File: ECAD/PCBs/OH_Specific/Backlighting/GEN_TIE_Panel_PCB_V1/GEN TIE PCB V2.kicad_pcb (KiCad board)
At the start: 2 copper layers, 45.7 x 130.8 mm, 28 parts, among them J1 IN, J2 THRU

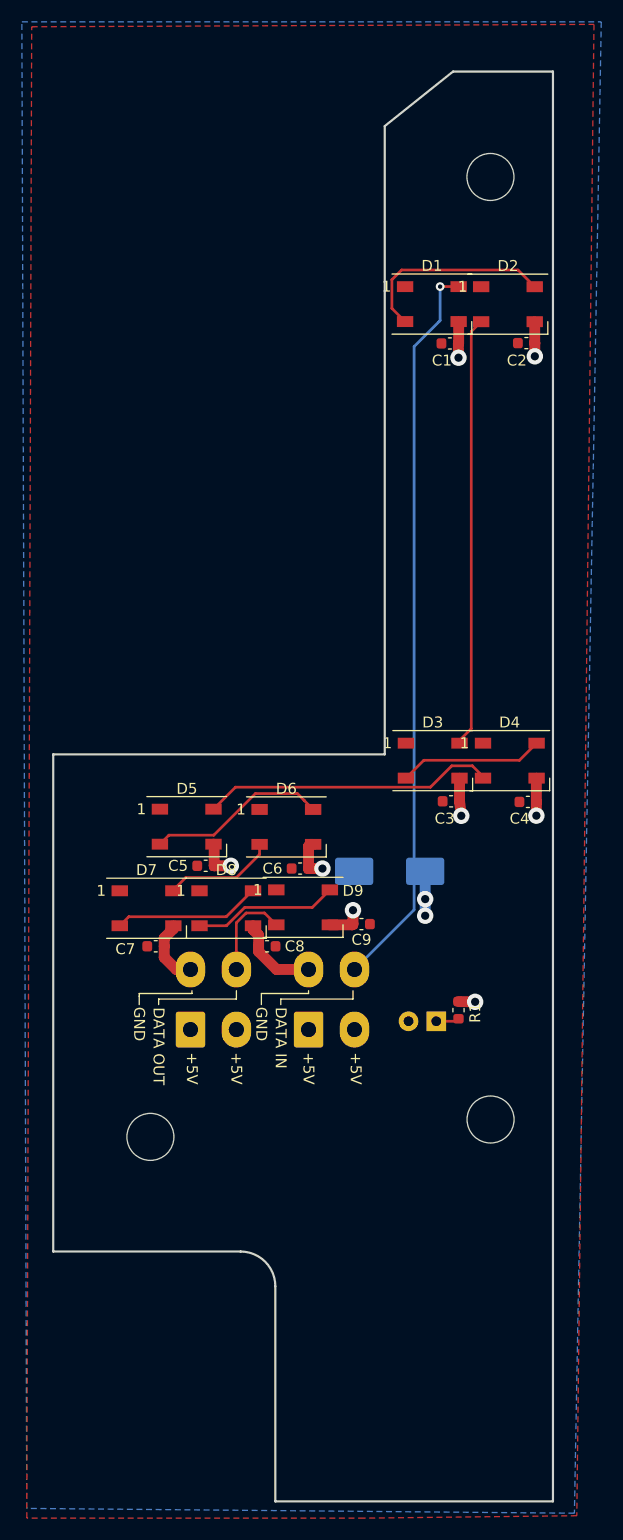
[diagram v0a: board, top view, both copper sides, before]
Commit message: GEN TIE Panel Backlighting Update
Changed - Data in trace re-routed so as not go straight through the capacitor pad, shorting it to 5V.
Changed - Manufacturing files to match the update
Changed - Version from 1.0 to 2.1 to match the other PCBs range.
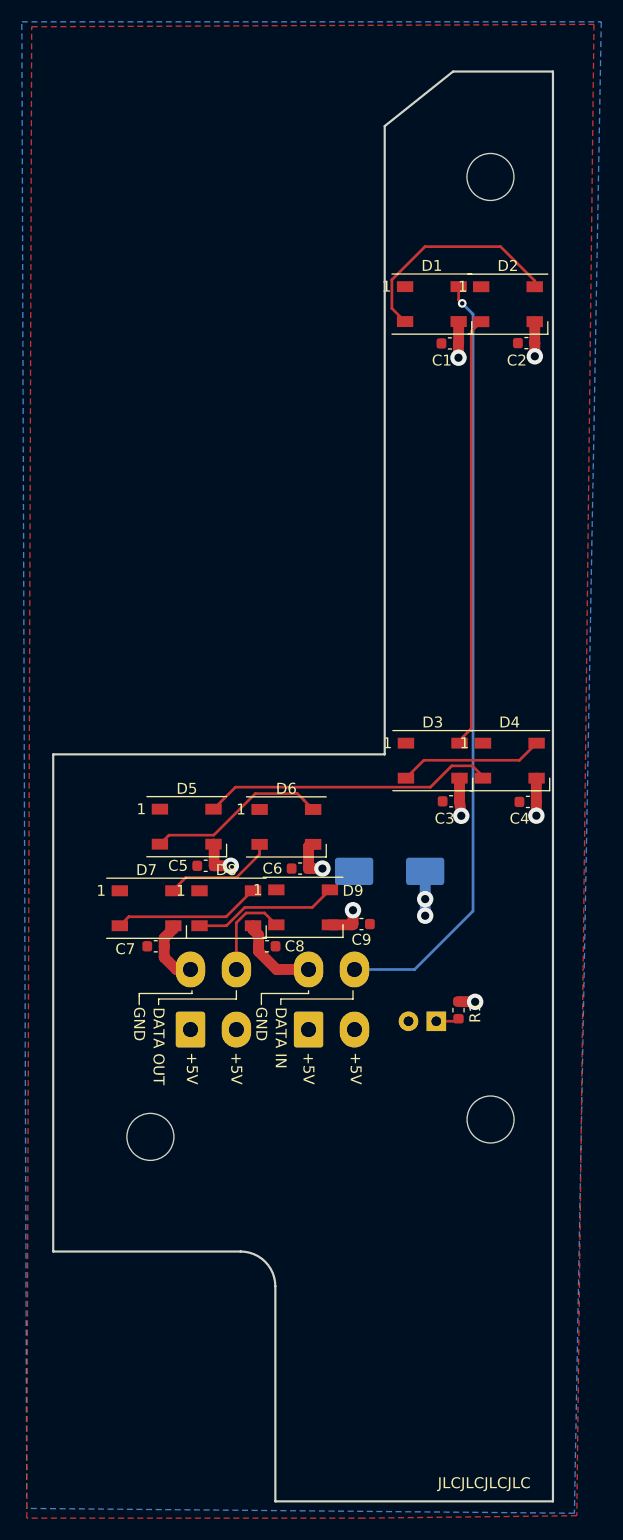
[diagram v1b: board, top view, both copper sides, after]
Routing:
- net /DATAIN: track 67.4 -> 70.7 mm
- net Net-(D1-Pad2): track 18.4 -> 20.5 mm
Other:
- board text added: "JLCJLCJLCJLC"
- board text added: "Version 2.1"
- board text removed: "Version 1.0"
